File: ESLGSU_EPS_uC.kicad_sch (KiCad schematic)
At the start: 111 parts, among them J4 Conn_01x06_Pin, J7 10118194-0001LF, U29 TCAN1051GVDRBRQ, U30 THVD1450DRBR, U31 TMUX1574RSVR, U32 TMUX1574RSVR, U33 TXU0202DTTR, U34 TMUX1574RSVR, U35 TXU0202DTTR, U37 STM32H743ZITx, U39 FXMA2102L8X, U44 TMUX1574RSVR, U46 TXB0104RUT, U47 TMUX1574RSVR, U52 TPS2115ADRBR, U56 TPS2115ADRBR, U57 CY8C9520A, U73 TPS2115ADRBR, U74 PCAL6524HEAZ, U81 ESD7004MUTAG, Y4 CSTNE8M00G55A

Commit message: Finished for production
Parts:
- U52, U56, U73: footprint Package_SON:VSON-8-1EP_3x3mm_P0.65mm_EP1.65x2.4mm_ThermalVias -> Package_SON:VSON-8-1EP_3x3mm_P0.65mm_EP1.65x2.4mm
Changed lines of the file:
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@@
       (effects (font (size 1.27 1.27)))
     )
-    (property "Footprint" "Package_SON:VSON-8-1EP_3x3mm_P0.65mm_EP1.65x2.4mm_ThermalVias" (at 193.04 193.04 0)
+    (property "Footprint" "Package_SON:VSON-8-1EP_3x3mm_P0.65mm_EP1.65x2.4mm" (at 193.04 193.04 0)
       (effects (font (size 1.27 1.27)) hide)
     )
@@
       (effects (font (size 1.27 1.27)))
     )
-    (property "Footprint" "Package_SON:VSON-8-1EP_3x3mm_P0.65mm_EP1.65x2.4mm_ThermalVias" (at 187.96 266.7 0)
+    (property "Footprint" "Package_SON:VSON-8-1EP_3x3mm_P0.65mm_EP1.65x2.4mm" (at 187.96 266.7 0)
       (effects (font (size 1.27 1.27)) hide)
     )
@@
       (effects (font (size 1.27 1.27)))
     )
-    (property "Footprint" "Package_SON:VSON-8-1EP_3x3mm_P0.65mm_EP1.65x2.4mm_ThermalVias" (at 187.96 236.22 0)
-      (effects (font (size 1.27 1.27)) hide)
-    )
+    (property "Footprint" "Package_SON:VSON-8-1EP_3x3mm_P0.65mm_EP1.65x2.4mm" (at 187.96 236.22 0)
+      (effects (font (size 1.27 1.27)) hide)
+    )

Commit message: Replaced netwroks with individual resistors
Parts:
- removed RN1, RN3, RN4: 0R, Resistor_SMD:R_Array_Concave_4x0402, symbol Device:R_Pack04
- removed RN2, RN5, RN6 (x2): 0R, Resistor_SMD:R_Array_Convex_2x0402, symbol Device:R_Pack02
- removed RN7: 10K, Resistor_SMD:R_Array_Convex_2x0402, symbol Device:R_Pack02
- added R10 (x2): 10K, Resistor_SMD:R_0402_1005Metric, symbol Device:R_Small_US
- added R6 (x20): 0R, Resistor_SMD:R_0402_1005Metric, symbol Device:R_Small_US
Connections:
- net CFGI2C_SCL: now also R6.1
- net CFGI2C_SDA: now also R6.1
- net EPS_I2C_SCL: now also R6.2
- net EPS_I2C_SDA: now also R6.2
- net GPIO_1: now also R6.1
- net GPIO_2: now also R6.1
- net GPIO_3: now also R6.1
- net GPIO_4: now also R6.1
- net GPIO_5: now also R6.1
- net GPIO_6: now also R6.1
- net GPIO_7: now also R6.1
- net GPIO_8: now also R6.1
- net I2C1_SCL: now also R10.1, R6.1
- net I2C1_SDA: now also R10.1, R6.1
- net RS4851_RX: now also R6.2
- net RS4851_TX: now also R6.2
- net SPI1_MISO: now also R6.1
- net SPI1_MOSI: now also R6.1
- net SPI1_NSS: now also R6.1
- net SPI1_SCK: now also R6.1
- net UART1_RX: now also R6.1
- net UART1_TX: now also R6.1
- net VBUS: now also R10.2, R10.2
- net _GPIO_1: now also R6.2
- net _GPIO_2: now also R6.2
- net _GPIO_3: now also R6.2
- net _GPIO_4: now also R6.2
- net _GPIO_5: now also R6.2
- net _GPIO_6: now also R6.2
- net _GPIO_7: now also R6.2
- net _GPIO_8: now also R6.2
- net _I2C1_SCL: now also R6.2
- net _I2C1_SDA: now also R6.2
- net _SPI1_MISO: now also R6.2
- net _SPI1_MOSI: now also R6.2
- net _SPI1_NSS: now also R6.2
- net _SPI1_SCK: now also R6.2
- net _UART1_RX: now also R6.2
- net _UART1_TX: now also R6.2
- net at U30.1 (R), U33.1 (B2): now also R6.1
- net at U30.4 (D), U33.8 (B1Y): now also R6.1

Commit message: Revert "Replaced netwroks with individual resistors"
This reverts commit e13850981b8de489d340064652a5562029ab4f8c.
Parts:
- removed R10 (x2): 10K, Resistor_SMD:R_0402_1005Metric, symbol Device:R_Small_US
- removed R6 (x20): 0R, Resistor_SMD:R_0402_1005Metric, symbol Device:R_Small_US
- added RN1, RN3, RN4: 0R, Resistor_SMD:R_Array_Concave_4x0402, symbol Device:R_Pack04
- added RN2, RN5, RN6 (x2): 0R, Resistor_SMD:R_Array_Convex_2x0402, symbol Device:R_Pack02
- added RN7: 10K, Resistor_SMD:R_Array_Convex_2x0402, symbol Device:R_Pack02
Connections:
- net CFGI2C_SCL: now also RN6.1 (R1.1)
- net CFGI2C_SDA: now also RN6.2 (R2.1)
- net EPS_I2C_SCL: now also RN6.4 (R1.2)
- net EPS_I2C_SDA: now also RN6.3 (R2.2)
- net GPIO_1: now also RN3.4 (R4.1)
- net GPIO_2: now also RN3.3 (R3.1)
- net GPIO_3: now also RN3.2 (R2.1)
- net GPIO_4: now also RN3.1 (R1.1)
- net GPIO_5: now also RN4.4 (R4.1)
- net GPIO_6: now also RN4.3 (R3.1)
- net GPIO_7: now also RN4.2 (R2.1)
- net GPIO_8: now also RN4.1 (R1.1)
- net I2C1_SCL: now also RN6.2 (R2.1), RN7.3 (R2.2)
- net I2C1_SDA: now also RN6.1 (R1.1), RN7.4 (R1.2)
- net RS4851_RX: now also RN5.4 (R1.2)
- net RS4851_TX: now also RN5.3 (R2.2)
- net SPI1_MISO: now also RN1.1 (R1.1)
- net SPI1_MOSI: now also RN1.4 (R4.1)
- net SPI1_NSS: now also RN1.2 (R2.1)
- net SPI1_SCK: now also RN1.3 (R3.1)
- net UART1_RX: now also RN2.1 (R1.1)
- net UART1_TX: now also RN2.2 (R2.1)
- net VBUS: now also RN7.1 (R1.1), RN7.2 (R2.1)
- net _GPIO_1: now also RN3.5 (R4.2)
- net _GPIO_2: now also RN3.6 (R3.2)
- net _GPIO_3: now also RN3.7 (R2.2)
- net _GPIO_4: now also RN3.8 (R1.2)
- net _GPIO_5: now also RN4.5 (R4.2)
- net _GPIO_6: now also RN4.6 (R3.2)
- net _GPIO_7: now also RN4.7 (R2.2)
- net _GPIO_8: now also RN4.8 (R1.2)
- net _I2C1_SCL: now also RN6.3 (R2.2)
- net _I2C1_SDA: now also RN6.4 (R1.2)
- net _SPI1_MISO: now also RN1.8 (R1.2)
- net _SPI1_MOSI: now also RN1.5 (R4.2)
- net _SPI1_NSS: now also RN1.7 (R2.2)
- net _SPI1_SCK: now also RN1.6 (R3.2)
- net _UART1_RX: now also RN2.4 (R1.2)
- net _UART1_TX: now also RN2.3 (R2.2)
- net at U30.1 (R), U33.1 (B2): now also RN5.1 (R1.1)
- net at U30.4 (D), U33.8 (B1Y): now also RN5.2 (R2.1)

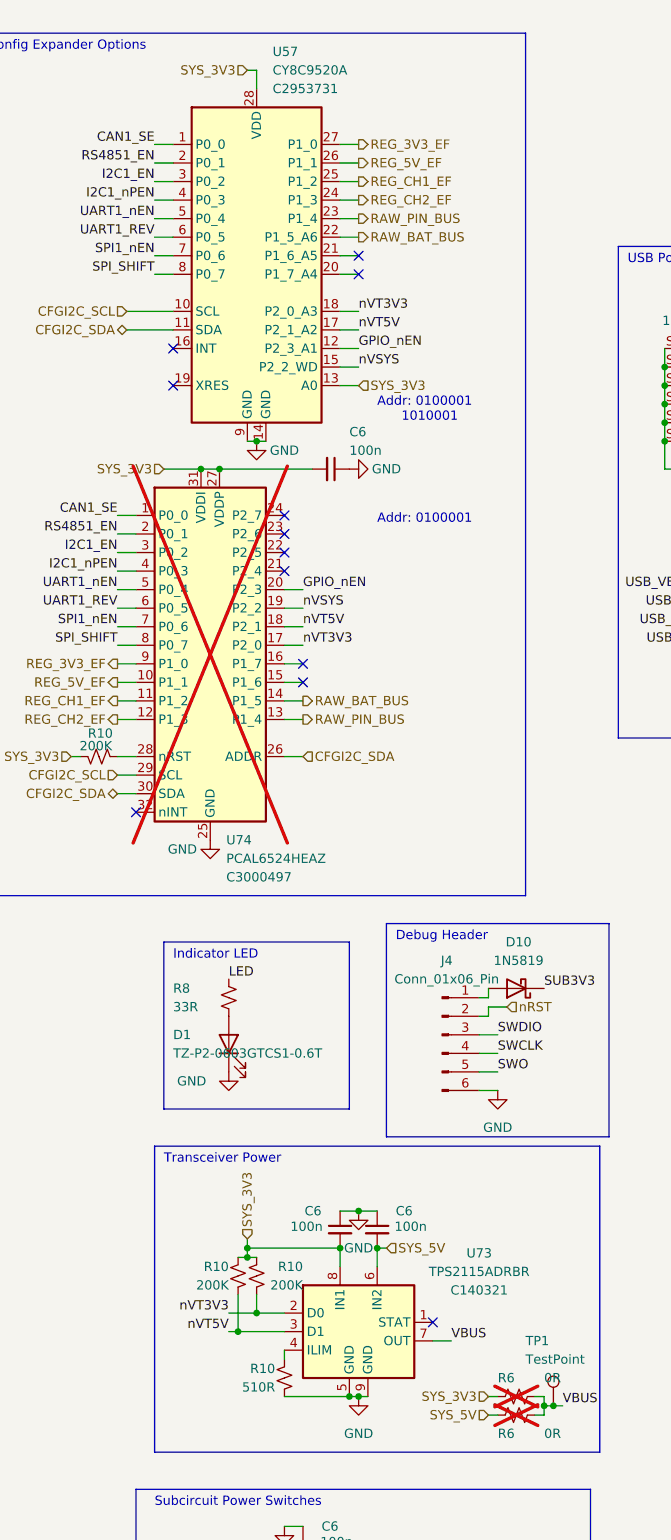
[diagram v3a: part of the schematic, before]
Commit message: Removed some parts
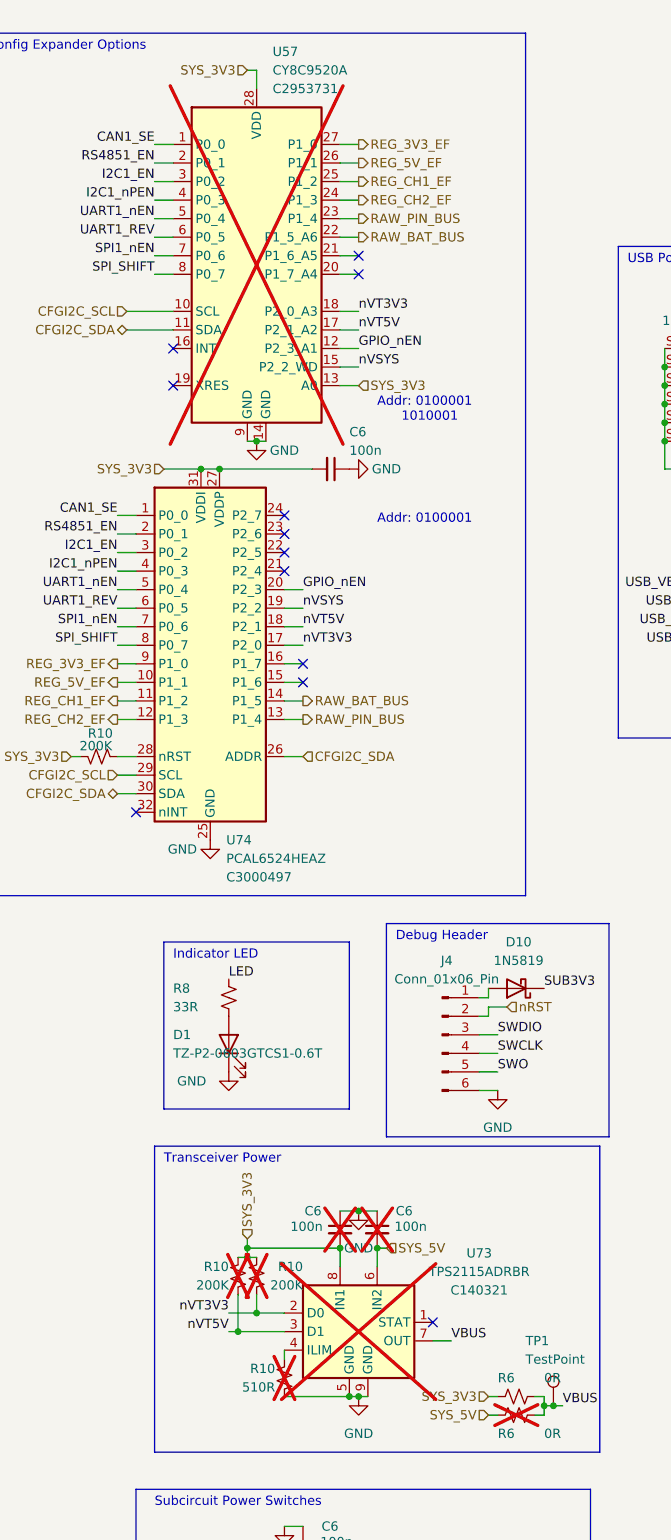
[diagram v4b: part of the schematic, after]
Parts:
- removed C6 (x2): 100n, Capacitor_SMD:C_0402_1005Metric, symbol Device:C_Small
- removed R10: 510R, Resistor_SMD:R_0402_1005Metric, symbol Device:R_Small_US
- removed R10 (x2): 200K, Resistor_SMD:R_0402_1005Metric, symbol Device:R_Small_US
- added C6 (x2): 100n, Capacitor_SMD:C_0402_1005Metric, symbol Device:C_Small
- added R10 (x2): 200K, Resistor_SMD:R_0402_1005Metric, symbol Device:R_Small_US
- added R10: 510R, Resistor_SMD:R_0402_1005Metric, symbol Device:R_Small_US
- R6, U74: now fitted; now in the parts list
- U57, U73: now not fitted; now left out of the parts list
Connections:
- net GND: now also C6.1, C6.1, R10.2
- net SYS_3V3: now also C6.2, R10.1, R10.1
- net SYS_5V: now also C6.2
- net nVT3V3: now also R10.2
- net nVT5V: now also R10.2
- net at U73.4 (ILIM): now also R10.1
